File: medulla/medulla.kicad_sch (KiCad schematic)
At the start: 0 parts

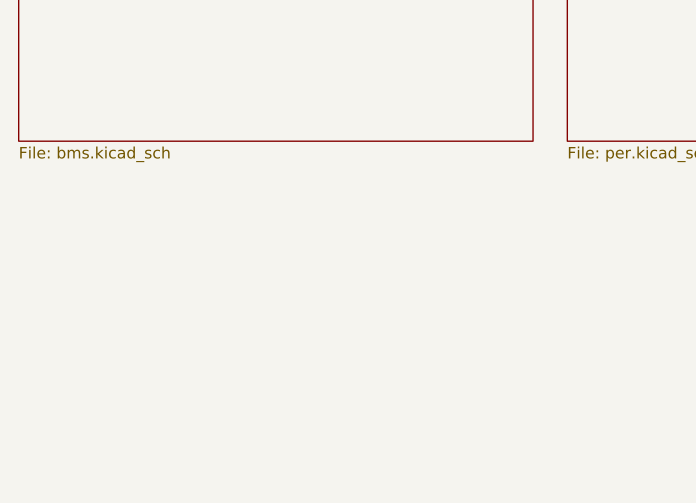
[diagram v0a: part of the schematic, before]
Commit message: alpha 0.2.0: Added RP2040, LM2936-3.3V Regulator, removed ADS1115, PCA9685
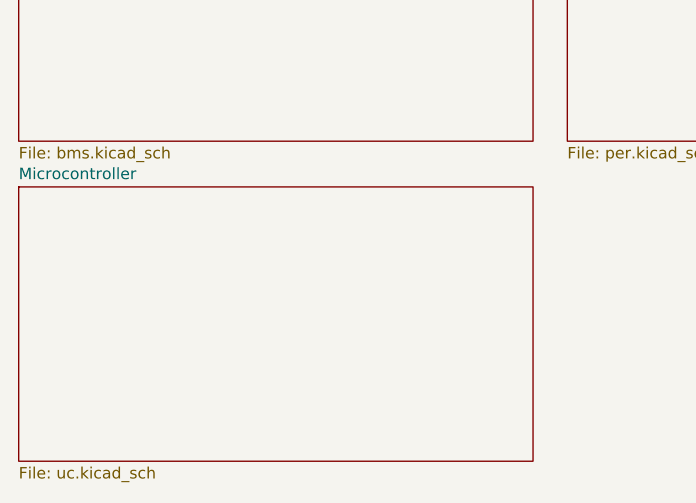
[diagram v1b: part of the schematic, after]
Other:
- added sheet Microcontroller (uc.kicad_sch)
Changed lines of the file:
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@@
+	)
+	(sheet
+		(at 17.78 87.63)
+		(size 57.15 30.48)
+		(exclude_from_sim no)
+		(in_bom yes)
+		(on_board yes)
+		(dnp no)
+		(fields_autoplaced yes)
+		(stroke
+			(width 0.1524)
+			(type solid)
+		)
+		(fill
+			(color 0 0 0 0.0000)
+		)
+		(property "Sheetname" "Microcontroller"
+			(at 17.78 86.9184 0)
+			(effects
+				(font
+					(size 1.27 1.27)
+				)
+				(justify left bottom)
+			)
+		)
+		(property "Sheetfile" "uc.kicad_sch"
+			(at 17.78 118.6946 0)
+			(effects
+				(font
+					(size 1.27 1.27)
+				)
+				(justify left top)
+			)
+		)
+		(property "Field2" ""
+			(at 17.78 87.63 0)
+			(effects
+				(font
+					(size 1.27 1.27)
+				)
+			)
+		)
+		(instances
+			(project "medulla"
+				(path "/d5881702-98ec-4aea-8d9c-3c163ba85aa3"
+					(page "8")
+				)
+			)
+		)
 	)
 	(sheet
